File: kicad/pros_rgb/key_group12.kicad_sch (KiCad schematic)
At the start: 16 parts

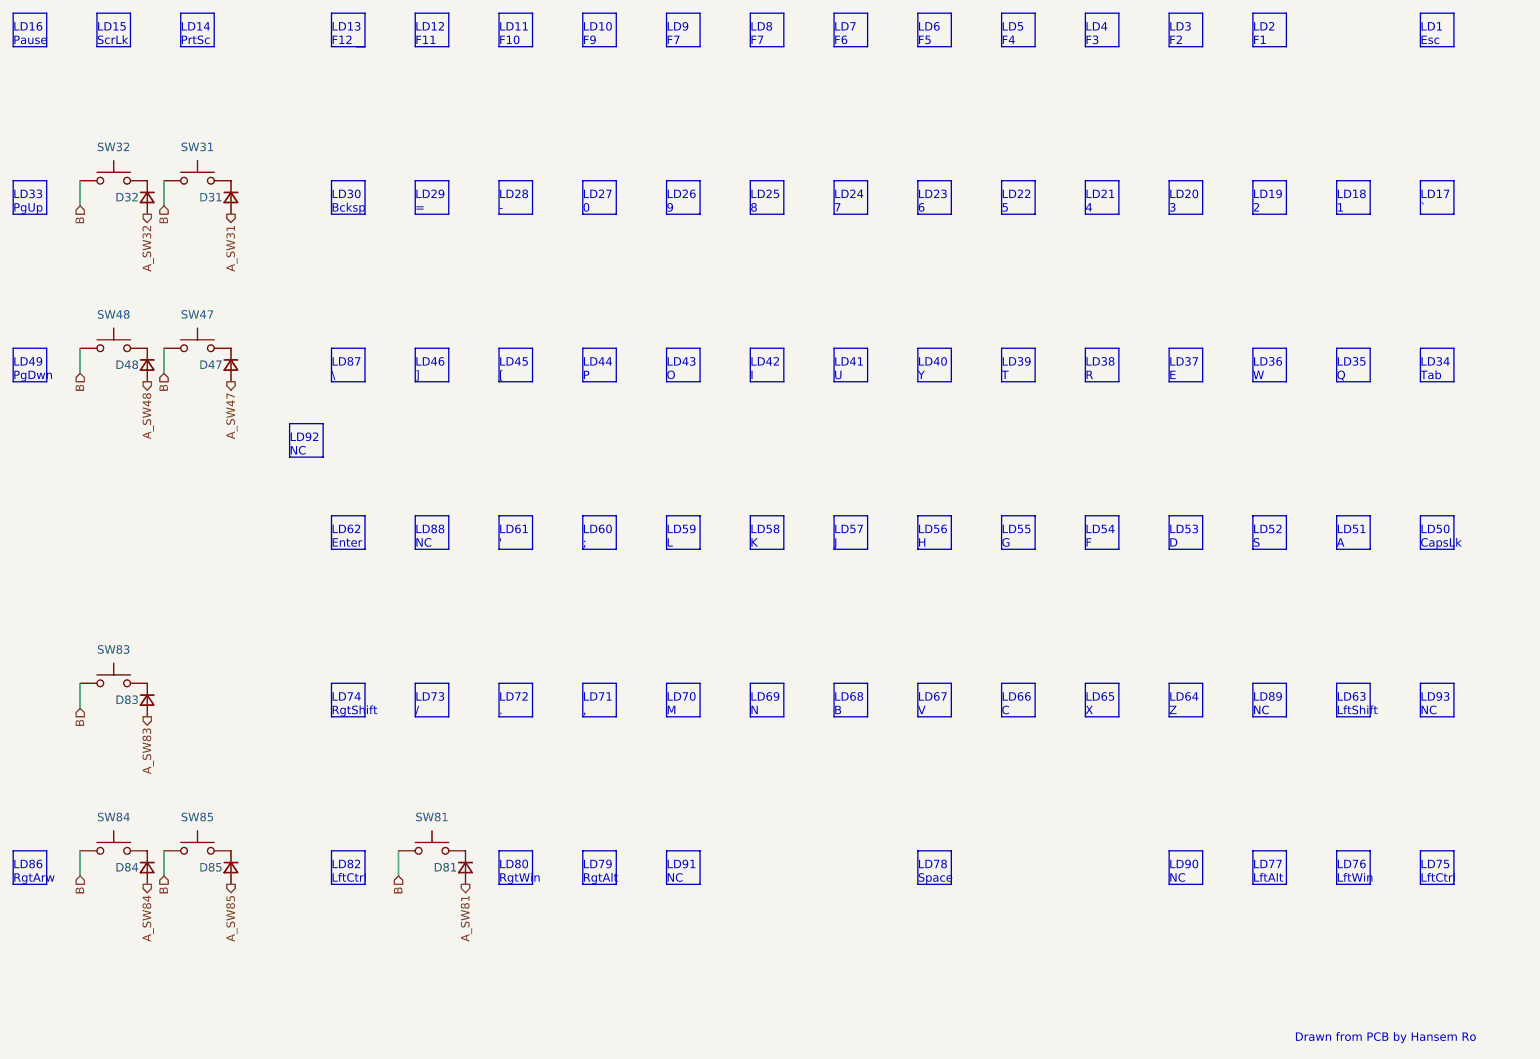
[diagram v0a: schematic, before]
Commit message: kicad/pros_rgb: update key groupings
These new groupings are based off ordering in firmware:
https://github.com/hansemro/pok3r_re_firmware/blob/4b68aa4baf7d28dc8dbf8eebcb1fdb59e7bcd629/disassemble/cmprosrgb/v122/cmprosrgb_v122.txt#L14599-L14629
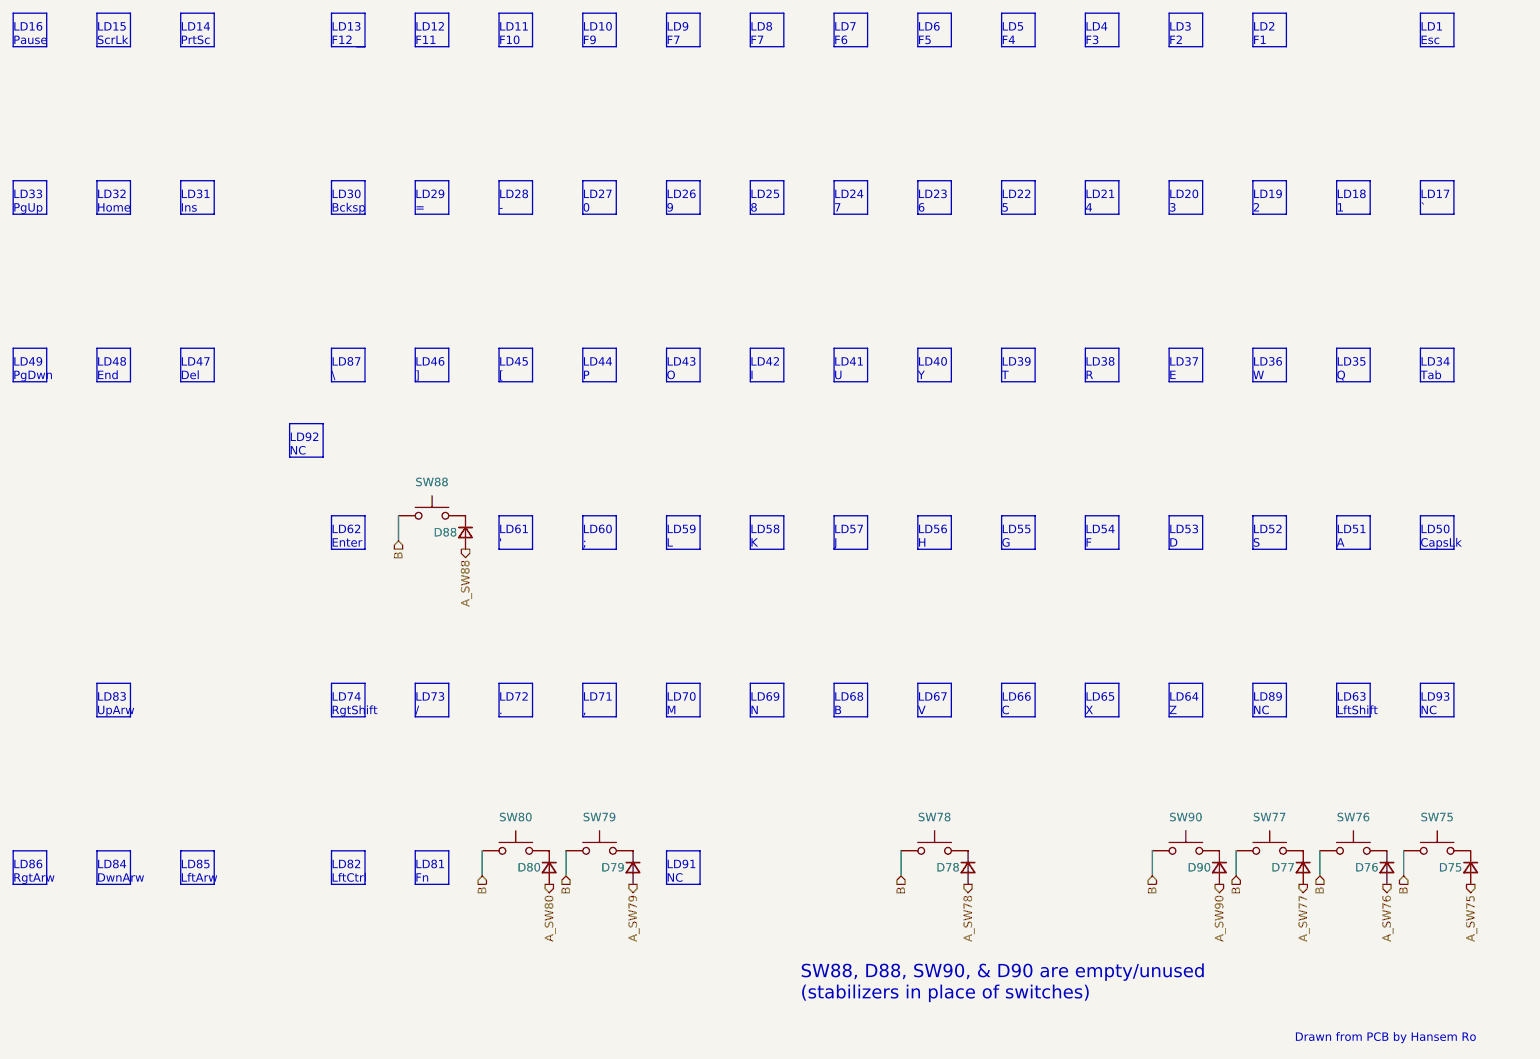
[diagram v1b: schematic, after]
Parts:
- removed D31, D32, D47, D48, D81, D83, D84, D85: ~, symbol Device:D_Small
- removed SW31, SW32, SW47, SW48, SW81, SW83, SW84, SW85: ~, symbol Switch:SW_Push
- added D75, D76, D77, D78, D79, D80, D88, D90: (no value), symbol Device:D_Small
- added SW75, SW76, SW77, SW78, SW79, SW80, SW88, SW90: (no value), symbol Switch:SW_Push
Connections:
- net B: now also SW75.1, SW76.1, SW77.1, SW78.1, SW79.1, SW80.1, SW88.1, SW90.1
- new net: D79.1 (K), SW79.2
- new net: D75.1 (K), SW75.2
- new net: D76.1 (K), SW76.2
- new net: D80.1 (K), SW80.2
- new net: D88.1 (K), SW88.2
- new net: D77.1 (K), SW77.2
- new net: D90.1 (K), SW90.2
- new net: D78.1 (K), SW78.2
- new net A_SW75: D75.2 (A)
- new net A_SW76: D76.2 (A)
- new net A_SW77: D77.2 (A)
- new net A_SW78: D78.2 (A)
- new net A_SW79: D79.2 (A)
- new net A_SW80: D80.2 (A)
- new net A_SW88: D88.2 (A)
- new net A_SW90: D90.2 (A)
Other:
- note added: "LD31 Ins"
- note added: "LD32 Home"
- note added: "LD47 Del"
- note added: "LD48 End"
- note added: "LD81 Fn"
- note added: "LD83 UpArw"
- note added: "LD84 DwnArw"
- note added: "LD85 LftArw"
- note added: "SW88, D88, SW90, & D90 are empty/unused (stabilizers in place of switches)"
- note removed: "LD75 LftCtrl"
- note removed: "LD76 LftWin"
- note removed: "LD77 LftAlt"
- note removed: "LD78 Space"
- note removed: "LD79 RgtAlt"
- note removed: "LD80 RgtWin"
- note removed: "LD88 NC"
- note removed: "LD90 NC"

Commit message: kicad/pros_rgb: mark as Rev. B
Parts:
- D75, D76, D77, D78, D79, D80, D88, D90, SW75, SW76, SW77, SW78, SW79, SW80, SW88, SW90: value (none) -> ~
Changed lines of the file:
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@@
       (effects (font (size 1.27 1.27)) (justify right))
     )
-    (property "Value" "" (id 1) (at 154.94 154.9399 90)
+    (property "Value" "~" (id 1) (at 154.94 154.9399 90)
       (effects (font (size 1.27 1.27)) (justify left))
     )
@@
       (effects (font (size 1.27 1.27)) (justify right))
     )
-    (property "Value" "" (id 1) (at 281.94 154.9399 90)
+    (property "Value" "~" (id 1) (at 281.94 154.9399 90)
       (effects (font (size 1.27 1.27)) (justify left))
     )
@@
     (in_bom yes) (on_board yes)
     (property "Reference" "SW76" (id 0) (at 261.62 146.05 0))
-    (property "Value" "" (id 1) (at 261.62 146.05 0))
+    (property "Value" "~" (id 1) (at 261.62 146.05 0))
     (property "Footprint" "" (id 2) (at 261.62 146.05 0)
       (effects (font (size 1.27 1.27)) hide)
@@
     (in_bom yes) (on_board yes)
     (property "Reference" "SW80" (id 0) (at 134.62 146.05 0))
-    (property "Value" "" (id 1) (at 134.62 146.05 0))
+    (property "Value" "~" (id 1) (at 134.62 146.05 0))
     (property "Footprint" "" (id 2) (at 134.62 146.05 0)
       (effects (font (size 1.27 1.27)) hide)
@@
       (effects (font (size 1.27 1.27)) (justify right))
     )
-    (property "Value" "" (id 1) (at 129.54 104.1399 90)
+    (property "Value" "~" (id 1) (at 129.54 104.1399 90)
       (effects (font (size 1.27 1.27)) (justify left))
     )
@@
     (in_bom yes) (on_board yes)
     (property "Reference" "SW77" (id 0) (at 248.92 146.05 0))
-    (property "Value" "" (id 1) (at 248.92 146.05 0))
+    (property "Value" "~" (id 1) (at 248.92 146.05 0))
     (property "Footprint" "" (id 2) (at 248.92 146.05 0)
       (effects (font (size 1.27 1.27)) hide)
@@
     (in_bom yes) (on_board yes)
     (property "Reference" "SW90" (id 0) (at 236.22 146.05 0))
-    (property "Value" "" (id 1) (at 236.22 146.05 0))
+    (property "Value" "~" (id 1) (at 236.22 146.05 0))
     (property "Footprint" "" (id 2) (at 236.22 146.05 0)
       (effects (font (size 1.27 1.27)) hide)
@@
     (in_bom yes) (on_board yes)
     (property "Reference" "SW78" (id 0) (at 198.12 146.05 0))
-    (property "Value" "" (id 1) (at 198.12 146.05 0))
+    (property "Value" "~" (id 1) (at 198.12 146.05 0))
     (property "Footprint" "" (id 2) (at 198.12 146.05 0)
       (effects (font (size 1.27 1.27)) hide)
@@
       (effects (font (size 1.27 1.27)) (justify right))
     )
-    (property "Value" "" (id 1) (at 243.84 154.9399 90)
+    (property "Value" "~" (id 1) (at 243.84 154.9399 90)
       (effects (font (size 1.27 1.27)) (justify left))
     )
@@
     (in_bom yes) (on_board yes)
     (property "Reference" "SW79" (id 0) (at 147.32 146.05 0))
-    (property "Value" "" (id 1) (at 147.32 146.05 0))
+    (property "Value" "~" (id 1) (at 147.32 146.05 0))
     (property "Footprint" "" (id 2) (at 147.32 146.05 0)
       (effects (font (size 1.27 1.27)) hide)
@@
       (effects (font (size 1.27 1.27)) (justify right))
     )
-    (property "Value" "" (id 1) (at 269.24 154.9399 90)
+    (property "Value" "~" (id 1) (at 269.24 154.9399 90)
       (effects (font (size 1.27 1.27)) (justify left))
     )
@@
     (in_bom yes) (on_board yes)
     (property "Reference" "SW75" (id 0) (at 274.32 146.05 0))
-    (property "Value" "" (id 1) (at 274.32 146.05 0))
+    (property "Value" "~" (id 1) (at 274.32 146.05 0))
     (property "Footprint" "" (id 2) (at 274.32 146.05 0)
       (effects (font (size 1.27 1.27)) hide)
@@
       (effects (font (size 1.27 1.27)) (justify right))
     )
-    (property "Value" "" (id 1) (at 142.24 154.9399 90)
+    (property "Value" "~" (id 1) (at 142.24 154.9399 90)
       (effects (font (size 1.27 1.27)) (justify left))
     )
@@
       (effects (font (size 1.27 1.27)) (justify right))
     )
-    (property "Value" "" (id 1) (at 256.54 154.9399 90)
+    (property "Value" "~" (id 1) (at 256.54 154.9399 90)
       (effects (font (size 1.27 1.27)) (justify left))
     )
@@
       (effects (font (size 1.27 1.27)) (justify right))
     )
-    (property "Value" "" (id 1) (at 205.74 154.9399 90)
+    (property "Value" "~" (id 1) (at 205.74 154.9399 90)
       (effects (font (size 1.27 1.27)) (justify left))
     )
@@
     (in_bom yes) (on_board yes)
     (property "Reference" "SW88" (id 0) (at 121.92 95.25 0))
-    (property "Value" "" (id 1) (at 121.92 95.25 0))
+    (property "Value" "~" (id 1) (at 121.92 95.25 0))
     (property "Footprint" "" (id 2) (at 121.92 95.25 0)
       (effects (font (size 1.27 1.27)) hide)

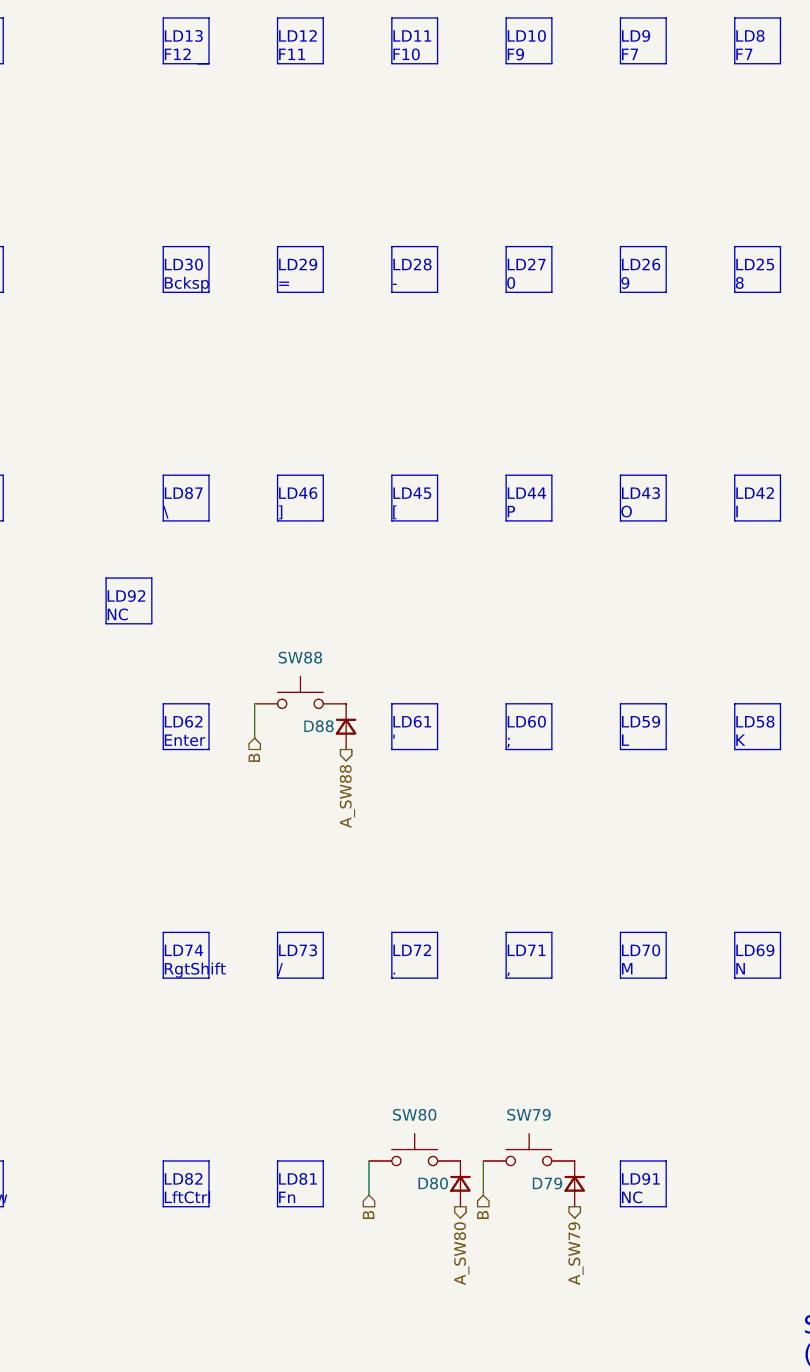
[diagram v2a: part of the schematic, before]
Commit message: kicad/pros_rgb: fix typos
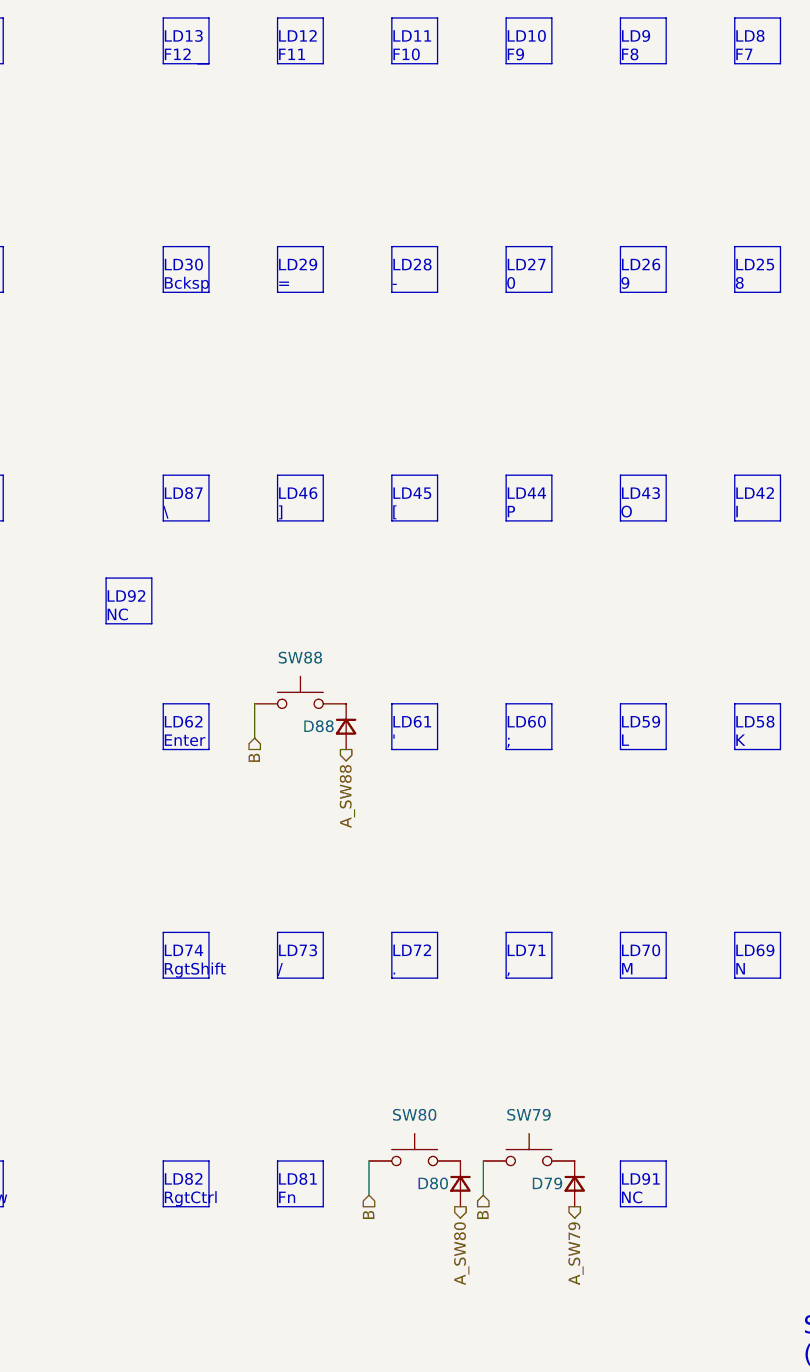
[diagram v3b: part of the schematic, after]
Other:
- note added: "LD82 RgtCtrl"
- note added: "LD9 F8"
- note removed: "LD82 LftCtrl"
- note removed: "LD9 F7"
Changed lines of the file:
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@@
     (effects (font (size 1.27 1.27)) (justify left bottom))
   )
-  (text "LD9\nF7" (at 157.48 29.21 0)
+  (text "LD9\nF8" (at 157.48 29.21 0)
     (effects (font (size 1.27 1.27)) (justify left bottom))
   )
@@
     (effects (font (size 1.27 1.27)) (justify left bottom))
   )
-  (text "LD82\nLftCtrl" (at 106.68 156.21 0)
+  (text "LD82\nRgtCtrl" (at 106.68 156.21 0)
     (effects (font (size 1.27 1.27)) (justify left bottom))
   )
